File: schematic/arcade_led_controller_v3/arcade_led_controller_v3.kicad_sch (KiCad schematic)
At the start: 64 parts, among them J1 GND_BUS_1, J2 GND_BUS_2, J3 PSU_GND_BUS, J4 Pico_Socket_Row_2, J5 Pico_Socket_Row_1, P1_BALLTOP_LED_1 WS2812B, P1_BUTTONS_LED1 WS2812B, P1_DP_JOY_MODE_LED1 LED, P1_JOYSTICK_LED1 WS2812B, P1_LS_JOY_MODE_LED1 LED, P1_RS_JOY_MODE_LED1 LED, P2_BALLTOP_LED_1 WS2812B, P2_BUTTONS_LED1 WS2812B, P2_DP_JOY_MODE_LED1 LED, P2_JOYSTICK_LED1 WS2812B, P2_LS_JOY_MODE_LED1 LED, P2_RS_JOY_MODE_LED1 LED, Q1 Q_NMOS_GDS, Q2 Q_NMOS_GDS, Q3 Q_NMOS_GDS, Q4(PN2222)1 PN2222A, Q5(PN222)1 PN2222A, Q6(PN2222)1 PN2222A, Q7(PN2222)1 PN2222A, SW1 RotaryEncoder_Switch, U1 74AHCT125, U2 74AHCT125, U3 EA_DOGL128X-6

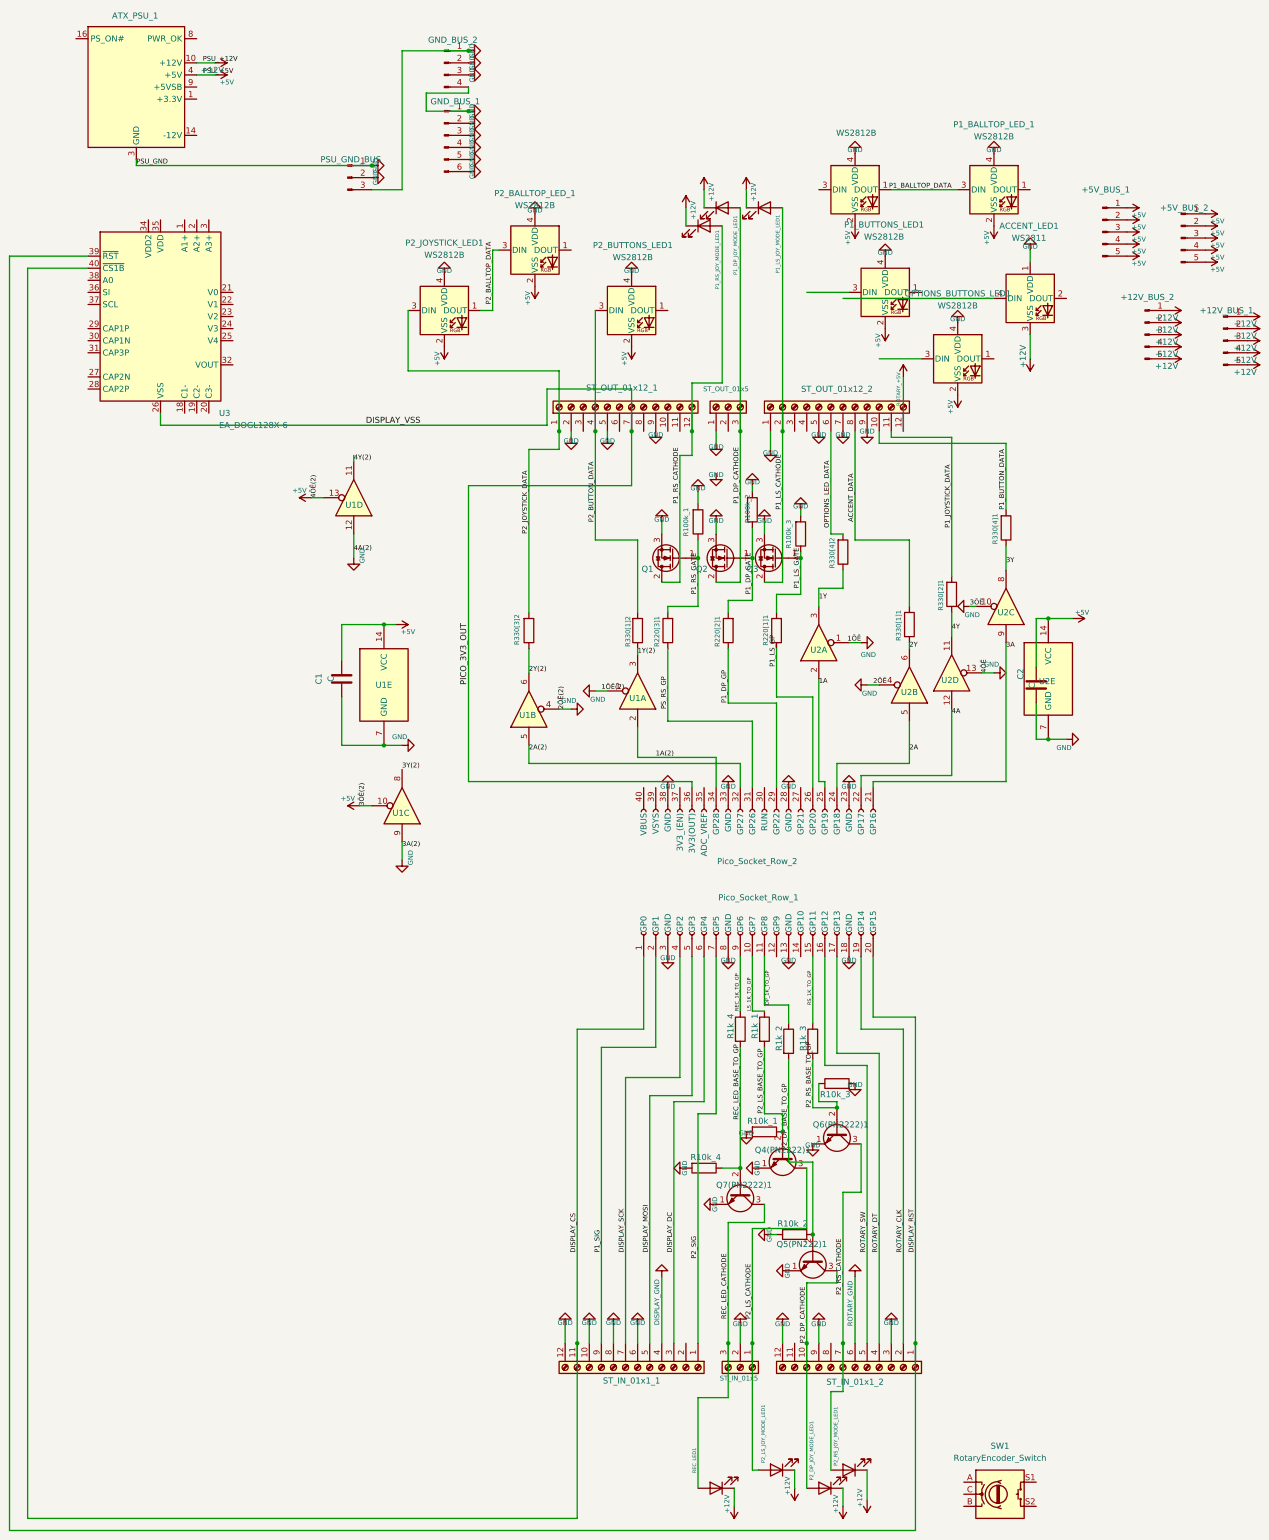
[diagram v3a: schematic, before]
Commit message: Add power LED connections, and replace pn2222 transistors with MOSFETs
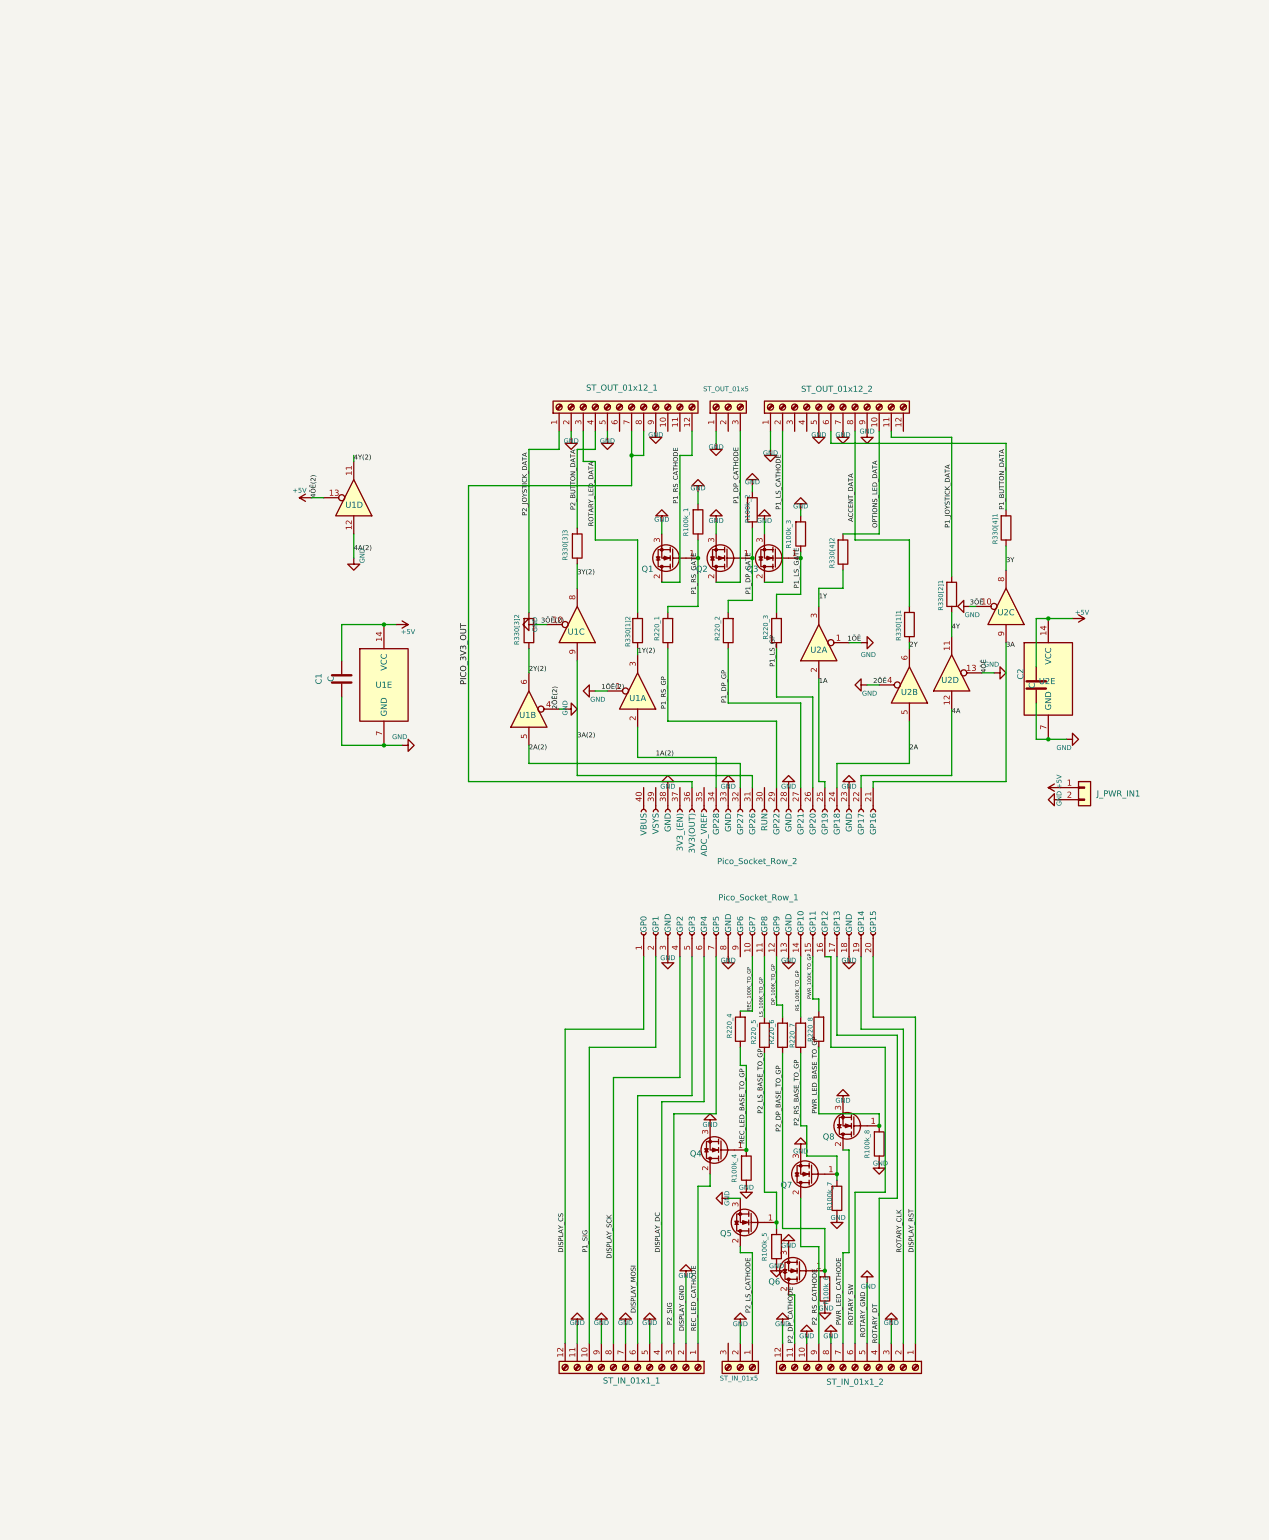
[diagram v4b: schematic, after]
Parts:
- removed +12V_BUS_1, +12V_BUS_2: Conn_01x05_Pin, TerminalBlock_WAGO:TerminalBlock_WAGO_233-505_2x05_P2.54mm, symbol Connector:Conn_01x05_Pin
- removed +5V_BUS_1, +5V_BUS_2: Conn_01x05_Pin, Connector_Wago:Wago_734-165_1x05_P3.50mm_Horizontal, symbol Connector:Conn_01x05_Pin
- removed ACCENT_LED1: WS2811, LED_SMD:LED_WS2812B_PLCC4_5.0x5.0mm_P3.2mm, symbol LED:WS2812B
- removed ATX_PSU_1: ATX-24, Connector_Molex:Molex_Mini-Fit_Jr_5566-24A_2x12_P4.20mm_Vertical, symbol Connector:ATX-24
- removed J1: GND_BUS_1, TerminalBlock_WAGO:TerminalBlock_WAGO_233-506_2x06_P2.54mm, symbol Connector:Conn_01x06_Pin
- removed J2: GND_BUS_2, TerminalBlock_WAGO:TerminalBlock_WAGO_233-504_2x04_P2.54mm, symbol Connector:Conn_01x04_Pin
- removed J3: PSU_GND_BUS, Connector_Wago:Wago_734-163_1x03_P3.50mm_Horizontal, symbol Connector:Conn_01x03_Pin
- removed OPTIONS_BUTTONS_LED1, P1_BALLTOP_LED_1, P1_BUTTONS_LED1, P1_JOYSTICK_LED1, P2_BALLTOP_LED_1, P2_BUTTONS_LED1, P2_JOYSTICK_LED1: WS2812B, LED_SMD:LED_WS2812B-2020_PLCC4_2.0x2.0mm, symbol LED:WS2812B-2020
- removed P1_DP_JOY_MODE_LED1, P1_LS_JOY_MODE_LED1, P1_RS_JOY_MODE_LED1, P2_DP_JOY_MODE_LED1, P2_LS_JOY_MODE_LED1, P2_RS_JOY_MODE_LED1, REC_LED1: LED, LED_THT:LED_D1.8mm_W1.8mm_H2.4mm_Horizontal_O3.81mm_Z1.6mm, symbol Device:LED
- removed Q4(PN2222)1, Q5(PN222)1, Q6(PN2222)1, Q7(PN2222)1: PN2222A, Package_TO_SOT_THT:TO-92_Inline_Wide, symbol Transistor_BJT:PN2222A
- removed R10k_1, R10k_2, R10k_3, R10k_4: 10kΩ, Resistor_THT:R_Axial_DIN0204_L3.6mm_D1.6mm_P5.08mm_Horizontal, symbol Device:R
- removed R1k_1, R1k_2, R1k_3, R1k_4: 1kΩ, Resistor_THT:R_Axial_DIN0204_L3.6mm_D1.6mm_P5.08mm_Horizontal, symbol Device:R
- removed SW1: RotaryEncoder_Switch, symbol Device:RotaryEncoder_Switch
- removed U3: EA_DOGL128X-6, Display:EA_DOGL128-6, symbol Display_Graphic:EA_DOGL128X-6
- added J_PWR_IN1: Conn_01x02, Connector_Molex:Molex_SL_171971-0002_1x02_P2.54mm_Vertical, symbol Connector_Generic:Conn_01x02
- added Q4, Q5, Q6, Q7, Q8: Q_NMOS_GDS, Package_TO_SOT_THT:TO-220-3_Vertical, symbol Transistor_FET:Q_NMOS_GDS
- added R100k_4, R100k_5, R100k_6, R100k_7, R100k_8: 100kΩ, Resistor_THT:R_Axial_DIN0204_L3.6mm_D1.6mm_P5.08mm_Horizontal, symbol Device:R
- added R220_4, R220_5, R220_6, R220_7, R220_8: 220Ω, Resistor_THT:R_Axial_DIN0204_L3.6mm_D1.6mm_P5.08mm_Horizontal, symbol Device:R
- added R330[3]3: 330Ω, Resistor_THT:R_Axial_DIN0204_L3.6mm_D1.6mm_P5.08mm_Horizontal, symbol Device:R
- renumbered R220[3]1 to R220_1, R220[2]1 to R220_2, R220[1]1 to R220_3
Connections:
- net DISPLAY_GND is gone; now on net DISPLAY_DC: ST_IN_01x1_1.4 (Pin_4)
- net DISPLAY_VSS is gone; now on net PICO_3V3_OUT: J4.36 (3V3(OUT)), ST_OUT_01x12_1.7 (Pin_7)
- net ROTARY_GND is gone; now on net ROTARY_SW: ST_IN_01x1_2.6 (Pin_6)
- net +5V: now also J_PWR_IN1.1 (Pin_1); no longer U1.10
- net 3Y(2): now also R330[3]3.1
- net DISPLAY_CS: now also ST_IN_01x1_1.12 (Pin_12); no longer ST_IN_01x1_1.11 (Pin_11)
- net DISPLAY_DC: no longer ST_IN_01x1_1.3 (Pin_3)
- net DISPLAY_MOSI: now also ST_IN_01x1_1.6 (Pin_6); no longer ST_IN_01x1_1.5 (Pin_5)
- net DISPLAY_SCK: now also ST_IN_01x1_1.8 (Pin_8); no longer ST_IN_01x1_1.7 (Pin_7)
- net GND: now also ST_IN_01x1_1.11 (Pin_11), ST_IN_01x1_1.2 (Pin_2), ST_IN_01x1_1.5 (Pin_5), ST_IN_01x1_1.7 (Pin_7), ST_IN_01x1_1.9 (Pin_9), ST_IN_01x1_2.10 (Pin_10), ST_IN_01x1_2.5 (Pin_5), ST_IN_01x1_2.8 (Pin_8), U1.10, J_PWR_IN1.2 (Pin_2), Q4.3 (S), Q5.3 (S), Q6.3 (S), Q7.3 (S), Q8.3 (S), R100k_4.1, R100k_5.1, R100k_6.1, R100k_7.1, R100k_8.1; no longer ST_IN_01x1_1.10 (Pin_10), ST_IN_01x1_1.12 (Pin_12), ST_IN_01x1_1.6 (Pin_6), ST_IN_01x1_1.8 (Pin_8), ST_IN_01x1_2.9 (Pin_9), U1.9
- net OPTIONS_LED_DATA: now also ST_OUT_01x12_2.10 (Pin_10); no longer ST_OUT_01x12_2.6 (Pin_6)
- net P1_BUTTON_DATA: now also ST_OUT_01x12_2.6 (Pin_6); no longer ST_OUT_01x12_2.10 (Pin_10)
- net P1_DP_GP: now also J4.27 (GP21); no longer J4.29 (GP22)
- net P1_SIG: now also ST_IN_01x1_1.10 (Pin_10); no longer ST_IN_01x1_1.9 (Pin_9)
- net P2_BUTTON_DATA: now also R330[3]3.2; no longer R330[1]2.2
- net P2_DP_BASE_TO_GP: now also Q6.1 (G), R100k_6.2, R220_6.1
- net P2_DP_CATHODE: now also ST_IN_01x1_2.11 (Pin_11), Q6.2 (D); no longer ST_IN_01x1_2.10 (Pin_10)
- net P2_LS_BASE_TO_GP: now also Q5.1 (G), R100k_5.2, R220_5.1
- net P2_LS_CATHODE: now also Q5.2 (D)
- net P2_RS_BASE_TO_GP: now also Q7.1 (G), R100k_7.2, R220_7.1
- net P2_RS_CATHODE: now also ST_IN_01x1_2.9 (Pin_9), Q7.2 (D); no longer ST_IN_01x1_2.7 (Pin_7)
- net P2_SIG: now also ST_IN_01x1_1.3 (Pin_3); no longer ST_IN_01x1_1.1 (Pin_1)
- net REC_LED_BASE_TO_GP: now also Q4.1 (G), R100k_4.2, R220_4.1
- net REC_LED_CATHODE: now also ST_IN_01x1_1.1 (Pin_1), Q4.2 (D); no longer ST_IN_01x5.3 (Pin_3)
- net ROTARY_SW: no longer ST_IN_01x1_2.5 (Pin_5)
- net ROTARY_LED_DATA: now reaches ST_OUT_01x12_1.3 (Pin_3)
- net ROTARY_LED_DATA: now also R330[1]2.2
- net PICO_3V3_OUT: now reaches ST_OUT_01x12_1.8 (Pin_8)
- net DP_100K_TO_GP: now reaches J5.12 (GP9)
- net DP_100K_TO_GP: now also R220_6.2
- net RS_100K_TO_GP: now reaches J5.14 (GP10)
- net RS_100K_TO_GP: now also R220_7.2
- net DP_1K_TO_GP renamed LS_100K_TO_GP
- net LS_100K_TO_GP: now also R220_5.2
- net LS_1K_TO_GP renamed REC_100K_TO_GP
- net REC_100K_TO_GP: now also R220_4.2
- net PS_RS_GP renamed 3A(2)
- net 3A(2): now also U1.9; no longer R220_1.1
- net REC_1K_TO_GP: no longer names the net of J5.9 (GP6)
- net ROTARY_+5V: no longer names the net of ST_OUT_01x12_2.12 (Pin_12)
- net RS_1K_TO_GP renamed PWR_100K_TO_GP
- net PWR_100K_TO_GP: now also R220_8.2
- new net P1_RS_GP: J4.29 (GP22), R220_1.1
- new net PWR_LED_BASE_TO_GP: Q8.1 (G), R100k_8.2, R220_8.1
- new net PWR_LED_CATHODE: Q8.2 (D), ST_IN_01x1_2.7 (Pin_7)
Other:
- moved on the sheet: U1C

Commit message: convert to SMD resistors, MOSFETs, and capacitors
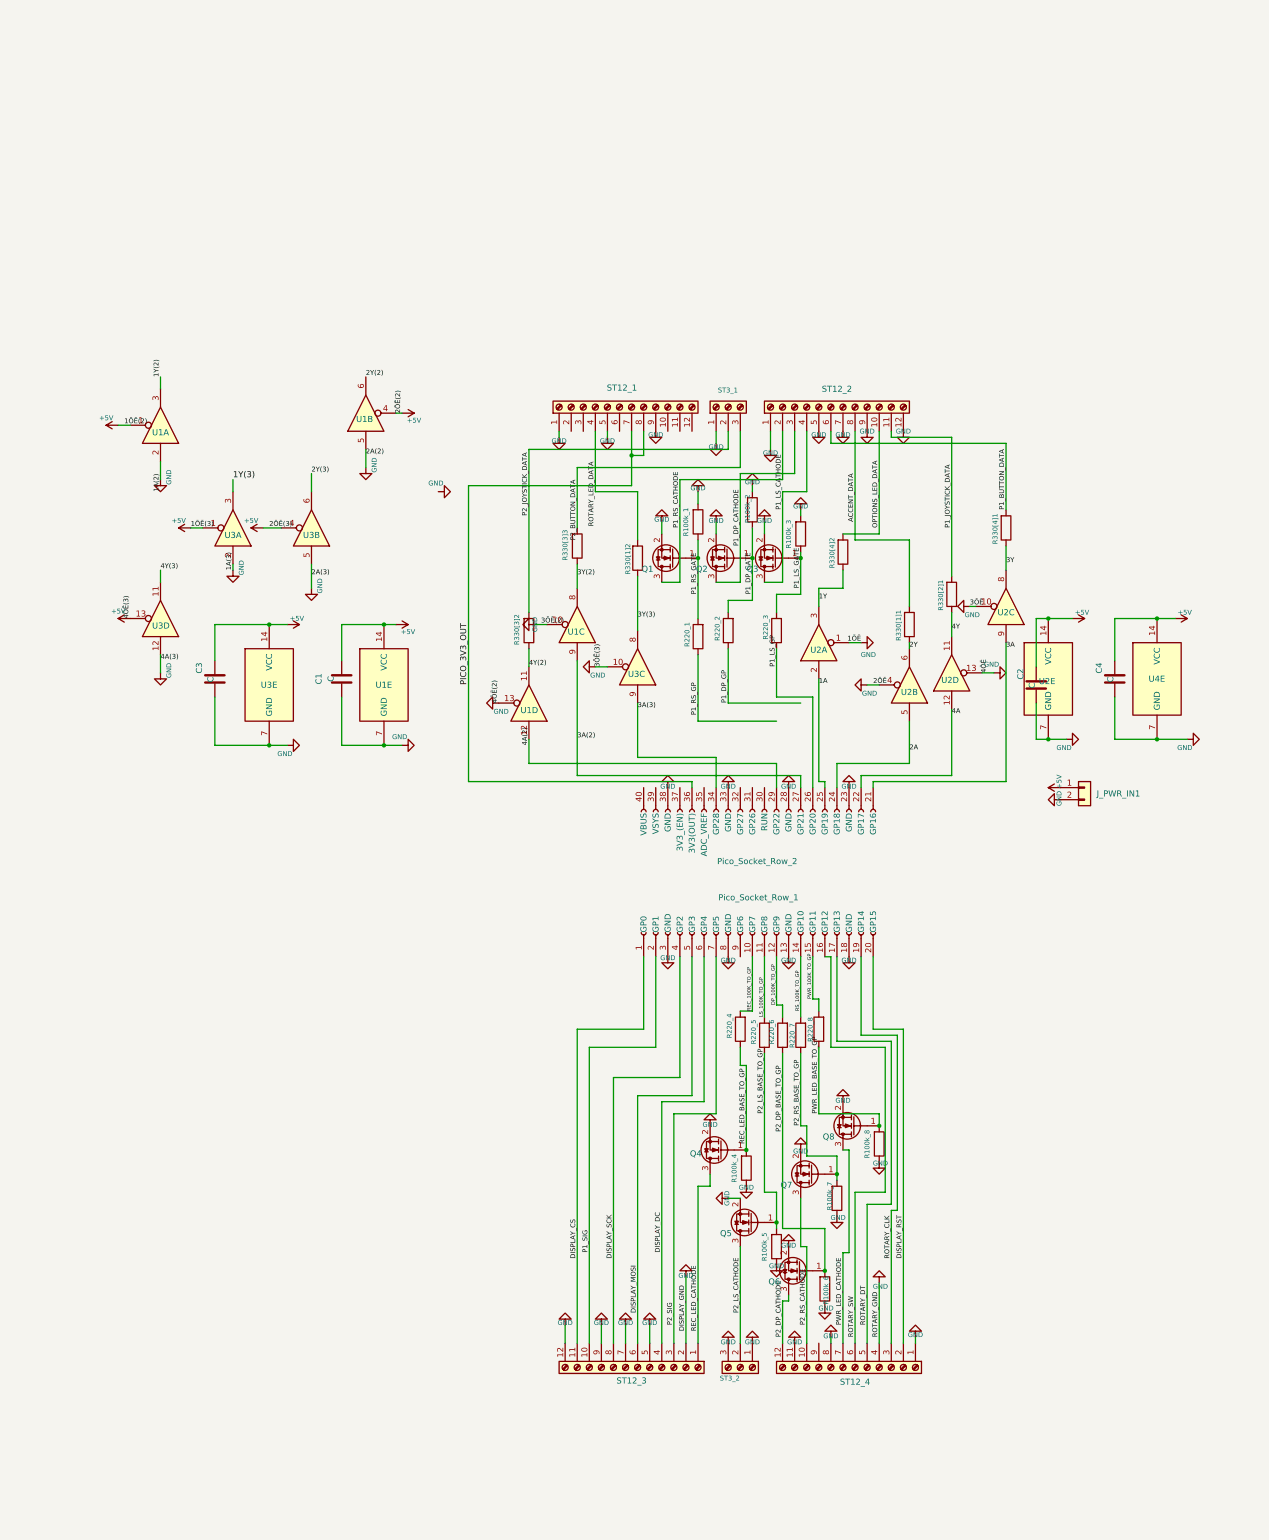
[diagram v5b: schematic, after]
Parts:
- added C3, C4: C, Capacitor_SMD:C_0805_2012Metric_Pad1.18x1.45mm_HandSolder, symbol Device:C
- added U3, U4: 74AHCT125, Package_SO:SOIC-14_3.9x8.7mm_P1.27mm, symbol 74xx:74AHCT125
- C1, C2: footprint Capacitor_THT:C_Disc_D3.0mm_W1.6mm_P2.50mm -> Capacitor_SMD:C_0805_2012Metric_Pad1.18x1.45mm_HandSolder
- J_PWR_IN1: footprint Connector_Molex:Molex_SL_171971-0002_1x02_P2.54mm_Vertical -> TerminalBlock_MetzConnect:TerminalBlock_MetzConnect_Type086_RT03402HBLC_1x02_P3.81mm_Horizontal
- Q1, Q2, Q3, Q4, Q5, Q6, Q7, Q8: footprint Package_TO_SOT_THT:TO-220-3_Vertical -> Package_TO_SOT_SMD:SOT-23; symbol Transistor_FET:Q_NMOS_GDS -> Transistor_FET:AO3400A
- R100k_1, R100k_2, R100k_3, R100k_4, R100k_5, R100k_6, R100k_7, R100k_8, R220_1, R220_2, R220_3, R220_4, R220_5, R220_6, R220_7, R220_8, R330[1]1, R330[1]2, R330[2]1, R330[3]2, R330[3]3, R330[4]1, R330[4]2: footprint Resistor_THT:R_Axial_DIN0204_L3.6mm_D1.6mm_P5.08mm_Horizontal -> Resistor_SMD:R_0805_2012Metric_Pad1.20x1.40mm_HandSolder
- ST12_1: renamed from ST_OUT_01x12_1; footprint TerminalBlock_Phoenix:TerminalBlock_Phoenix_MPT-0,5-12-2.54_1x12_P2.54mm_Horizontal -> TerminalBlock_TE-Connectivity:TerminalBlock_TE_1-282834-2_1x12_P2.54mm_Horizontal
- ST12_2: renamed from ST_OUT_01x12_2; footprint TerminalBlock_Phoenix:TerminalBlock_Phoenix_MPT-0,5-12-2.54_1x12_P2.54mm_Horizontal -> TerminalBlock_TE-Connectivity:TerminalBlock_TE_1-282834-2_1x12_P2.54mm_Horizontal
- ST12_3: renamed from ST_IN_01x1_1; footprint TerminalBlock_Phoenix:TerminalBlock_Phoenix_MPT-0,5-12-2.54_1x12_P2.54mm_Horizontal -> TerminalBlock_TE-Connectivity:TerminalBlock_TE_1-282834-2_1x12_P2.54mm_Horizontal
- ST12_4: renamed from ST_IN_01x1_2; footprint TerminalBlock_Phoenix:TerminalBlock_Phoenix_MPT-0,5-12-2.54_1x12_P2.54mm_Horizontal -> TerminalBlock_TE-Connectivity:TerminalBlock_TE_1-282834-2_1x12_P2.54mm_Horizontal
- ST3_1: renamed from ST_OUT_01x5; footprint TerminalBlock_Phoenix:TerminalBlock_Phoenix_MPT-0,5-3-2.54_1x03_P2.54mm_Horizontal -> TerminalBlock_TE-Connectivity:TerminalBlock_TE_282834-3_1x03_P2.54mm_Horizontal
- ST3_2: renamed from ST_IN_01x5; footprint TerminalBlock_Phoenix:TerminalBlock_Phoenix_MPT-0,5-3-2.54_1x03_P2.54mm_Horizontal -> TerminalBlock_TE-Connectivity:TerminalBlock_TE_282834-3_1x03_P2.54mm_Horizontal
- U1, U2: footprint Package_DIP:DIP-14_W7.62mm -> Package_SO:SOIC-14_3.9x8.7mm_P1.27mm
- U2: footprint (none) -> Package_SO:SOIC-14_3.9x8.7mm_P1.27mm
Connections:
- net +5V: now also U1.1, U1.4, C3.2, C4.2, U3.1, U3.13, U3.14 (VCC), U3.4, U4.14 (VCC); no longer U1.13
- net 1Y(2): no longer R330[1]2.1
- net 2Y(2): no longer R330[3]2.1
- net 3A(2): now also J4.27 (GP21); no longer J4.31 (GP26)
- net 4Y(2): now also R330[3]2.1
- net DISPLAY_CS: now also ST12_3.11 (Pin_11); no longer ST12_3.12 (Pin_12)
- net DISPLAY_RST: now also ST12_4.2 (Pin_2); no longer ST12_4.1 (Pin_1)
- net GND: now also Q1.2 (S), Q2.2 (S), Q3.2 (S), Q4.2 (S), Q5.2 (S), Q6.2 (S), Q7.2 (S), Q8.2 (S), ST12_1.1 (Pin_1), ST12_2.12 (Pin_12), ST12_3.12 (Pin_12), ST12_4.1 (Pin_1), ST12_4.11 (Pin_11), ST12_4.4 (Pin_4), ST3_2.1 (Pin_1), ST3_2.3 (Pin_3), U1.13, U1.2, U1.5, C3.1, C4.1, U3.10, U3.12, U3.2, U3.5, U3.7 (GND), U4.7 (GND); no longer Q1.3 (S), Q2.3 (S), Q3.3 (S), Q4.3 (S), Q5.3 (S), Q6.3 (S), Q7.3 (S), Q8.3 (S), ST12_1.2 (Pin_2), ST12_3.11 (Pin_11), ST12_4.10 (Pin_10), ST12_4.12 (Pin_12), ST12_4.3 (Pin_3), ST12_4.5 (Pin_5), ST3_2.2 (Pin_2), U1.1, U1.12, U1.4
- net P1_DP_CATHODE: now also Q2.3 (D), ST12_2.3 (Pin_3); no longer Q2.2 (D), ST3_1.3 (Pin_3)
- net P1_DP_GP: no longer J4.27 (GP21)
- net P1_LS_CATHODE: now also Q3.3 (D), ST12_2.4 (Pin_4); no longer Q3.2 (D), ST12_2.2 (Pin_2)
- net P1_RS_CATHODE: now also Q1.3 (D), ST12_2.2 (Pin_2); no longer Q1.2 (D), ST12_1.12 (Pin_12)
- net P1_RS_GP: no longer J4.29 (GP22)
- net P2_BUTTON_DATA: now also ST3_1.3 (Pin_3); no longer ST12_1.4 (Pin_4)
- net P2_DP_CATHODE: now also Q6.3 (D), ST12_4.12 (Pin_12); no longer Q6.2 (D), ST12_4.11 (Pin_11)
- net P2_JOYSTICK_DATA: now also ST3_1.2 (Pin_2); no longer ST12_1.1 (Pin_1)
- net P2_LS_CATHODE: now also Q5.3 (D), ST3_2.2 (Pin_2); no longer Q5.2 (D), ST3_2.1 (Pin_1)
- net P2_RS_CATHODE: now also Q7.3 (D), ST12_4.10 (Pin_10); no longer Q7.2 (D), ST12_4.9 (Pin_9)
- net PWR_LED_CATHODE: now also Q8.3 (D); no longer Q8.2 (D)
- net REC_LED_CATHODE: now also Q4.3 (D); no longer Q4.2 (D)
- net ROTARY_CLK: now also ST12_4.3 (Pin_3); no longer ST12_4.2 (Pin_2)
- net ROTARY_DT: now also ST12_4.5 (Pin_5); no longer ST12_4.4 (Pin_4)
- net ROTARY_LED_DATA: now also ST12_1.4 (Pin_4); no longer ST12_1.3 (Pin_3)
- net 1A(2) renamed 3A(3)
- net 3A(3): now also U3.9; no longer U1.2
- net 2A(2): no longer names the net of J4.32 (GP27)
- net 2A(2): no longer U1.5
- new net 1Y(3): U3.3
- new net 2Y(3): U3.6
- new net 3Y(3): R330[1]2.1, U3.8
- new net 4A(2): J4.29 (GP22), U1.12
- new net 4Y(3): U3.11
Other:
- moved on the sheet: R220_1, R330[1]2, U1A, U1B, U1D
